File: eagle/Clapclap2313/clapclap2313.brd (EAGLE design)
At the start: 47.9 x 48.2 mm, 20 parts, among them K1 4052, M1 Mic

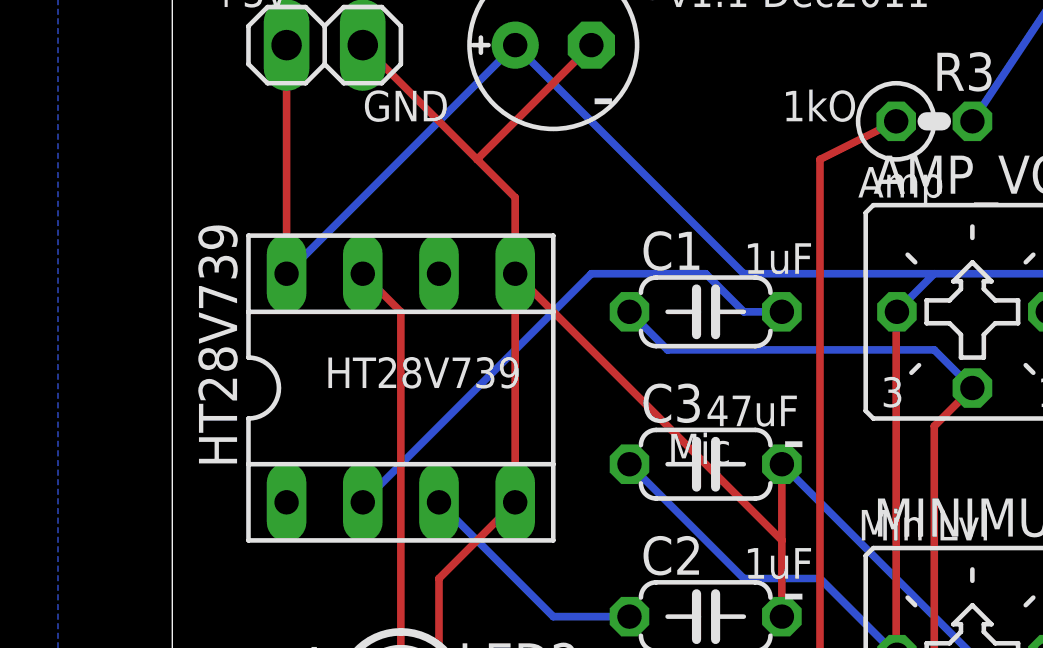
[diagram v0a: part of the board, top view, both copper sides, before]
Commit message: Thanks to Mr. Girts from Riga, the name of the amp is now fixed.
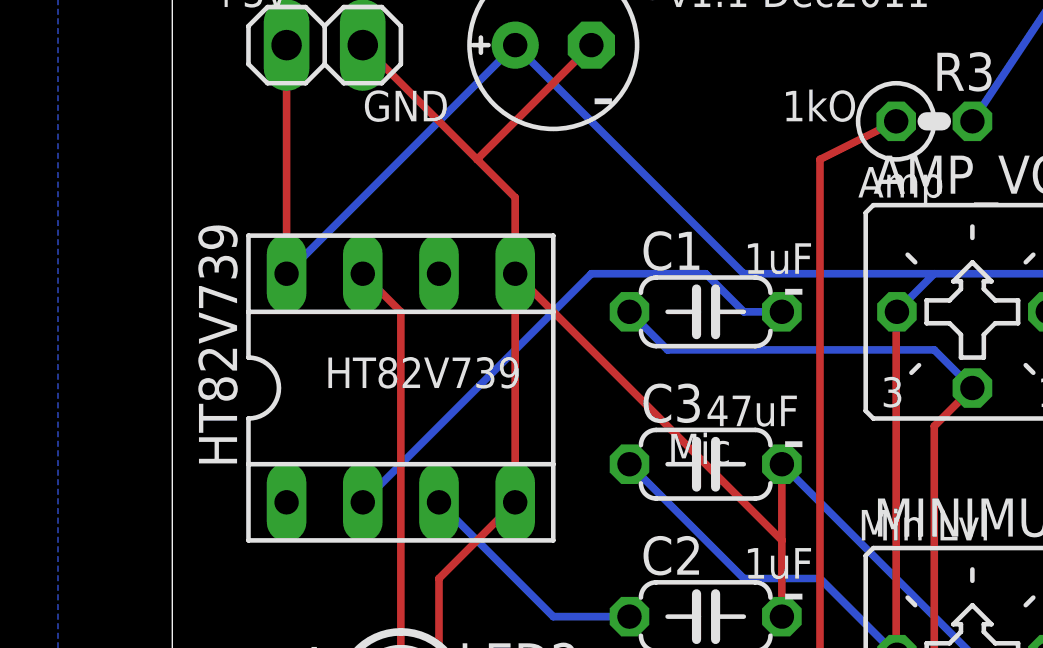
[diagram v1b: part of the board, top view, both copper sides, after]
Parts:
- renumbered HT28V739 to HT82V739
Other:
- board text added: "HT82V739"
- board text removed: "HT28V739"
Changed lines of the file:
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@@
 <text x="6.35" y="41.91" size="1.016" layer="21">GND</text>
 <text x="11.43" y="6.35" size="1.016" layer="21">ATtiny 2313</text>
-<text x="5.08" y="33.02" size="1.016" layer="21">HT28V739</text>
+<text x="5.08" y="33.02" size="1.016" layer="21">HT82V739</text>
 <text x="19.05" y="36.83" size="1.016" layer="21">1uF</text>
 <text x="19.05" y="26.67" size="1.016" layer="21">1uF</text>
@@
 <text x="15.24" y="15.24" size="1.016" layer="21" rot="R90">470o</text>
 <text x="19.05" y="15.24" size="1.016" layer="21" rot="R90">470o</text>
+<text x="20.32" y="35.56" size="1.778" layer="21">-</text>
 </plain>
 <attributes>
@@
 <attribute name="OC_NEWARK" value="unknown" x="16.51" y="6.35" size="1.778" layer="27" display="off"/>
 </element>
-<element name="HT28V739" library="ic-package" package="SOCKET-08" value="" x="7.62" y="33.02"/>
+<element name="HT82V739" library="ic-package" package="SOCKET-08" value="" x="7.62" y="33.02"/>
 <element name="M1" library="pinhead" package="1X02" value="Mic" x="27.94" y="15.24"/>
 <element name="NPN" library="transistor" package="TO92-ECB" value="2SC2120" x="39.37" y="43.18"/>
@@
 <signal name="N$5">
 <contactref element="C1" pad="2"/>
-<contactref element="HT28V739" pad="2"/>
+<contactref element="HT82V739" pad="2"/>
 <wire x1="6.35" y1="29.21" x2="13.97" y2="36.83" width="0.254" layer="16"/>
 <wire x1="13.97" y1="36.83" x2="17.78" y2="36.83" width="0.254" layer="16"/>
@@
 </signal>
 <signal name="N$10">
-<contactref element="HT28V739" pad="7"/>
+<contactref element="HT82V739" pad="7"/>
 <contactref element="ATTINY2313" pad="12"/>
 <wire x1="21.59" y1="6.35" x2="25.4" y2="10.16" width="0.254" layer="1"/>
@@
 <contactref element="AMP_VOL" pad="E"/>
 <contactref element="C3" pad="1"/>
-<contactref element="HT28V739" pad="8"/>
+<contactref element="HT82V739" pad="8"/>
 <contactref element="MINIMUM_LVL" pad="E"/>
 <contactref element="ATTINY2313" pad="20"/>
@@
 <contactref element="AMP_VOL" pad="A"/>
 <contactref element="M1" pad="2"/>
-<contactref element="HT28V739" pad="5"/>
+<contactref element="HT82V739" pad="5"/>
 <contactref element="C2" pad="2"/>
-<contactref element="HT28V739" pad="4"/>
+<contactref element="HT82V739" pad="4"/>
 <contactref element="C3" pad="2"/>
 <contactref element="MINIMUM_LVL" pad="A"/>
@@
 </signal>
 <signal name="N$1">
-<contactref element="HT28V739" pad="3"/>
+<contactref element="HT82V739" pad="3"/>
 <contactref element="C2" pad="1"/>
 <wire x1="8.89" y1="29.21" x2="12.7" y2="25.4" width="0.254" layer="16"/>

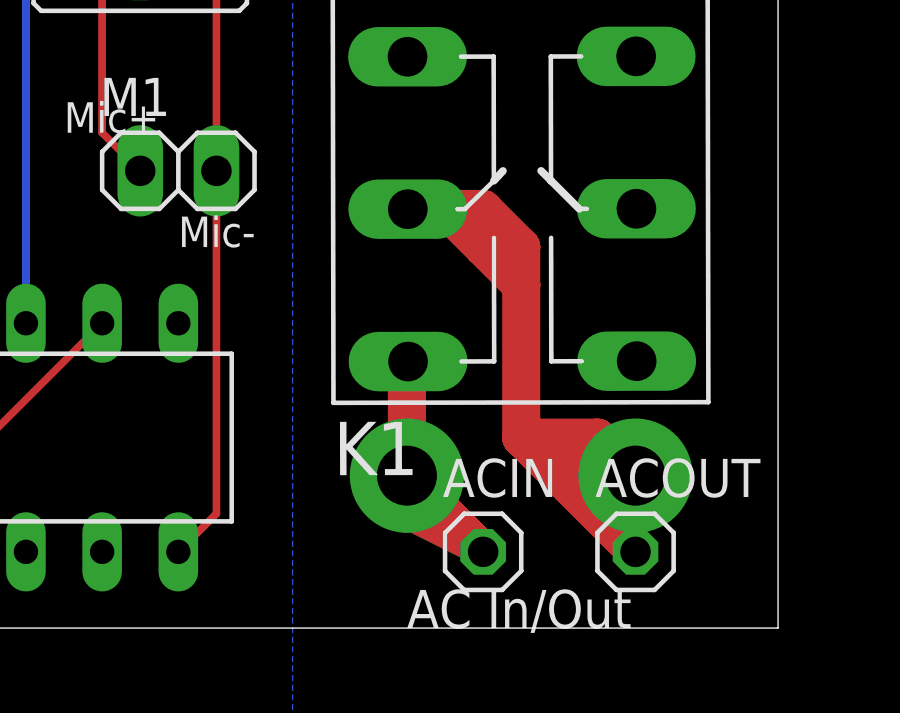
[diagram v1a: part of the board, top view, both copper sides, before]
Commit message: v1.1 final before v1.2. Changed width of some track. Will redo the whole board from scratch to save space in next version.
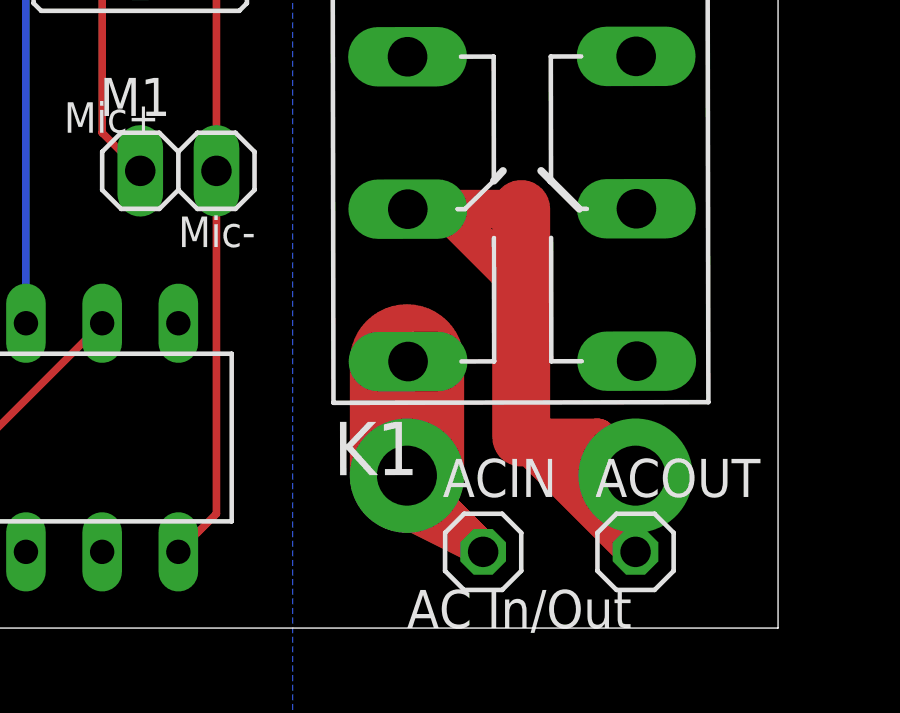
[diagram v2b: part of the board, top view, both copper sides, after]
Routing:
- net ACOUT: track 34.7 -> 31.4 mm
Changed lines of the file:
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@@
 <wire x1="35.56" y1="5.08" x2="35.56" y2="6.35" width="1.016" layer="1"/>
 <wire x1="35.56" y1="6.35" x2="35.597684375" y2="8.88338125" width="1.016" layer="1"/>
-<wire x1="35.56" y1="8.89" x2="35.56" y2="5.08" width="1.27" layer="1"/>
+<wire x1="35.56" y1="8.89" x2="35.56" y2="5.08" width="3.81" layer="1"/>
 <wire x1="35.56" y1="5.08" x2="35.56" y2="3.81" width="1.27" layer="1"/>
 <wire x1="35.56" y1="3.81" x2="36.83" y2="3.81" width="1.27" layer="1"/>
@@
 <wire x1="43.18" y1="2.54" x2="40.64" y2="5.08" width="1.016" layer="1"/>
 <wire x1="40.64" y1="5.08" x2="39.37" y2="6.35" width="1.016" layer="1"/>
-<wire x1="39.37" y1="12.7" x2="36.83" y2="13.97" width="1.016" layer="1"/>
 <wire x1="36.83" y1="13.97" x2="35.58881875" y2="13.963375" width="1.016" layer="1"/>
 <wire x1="39.37" y1="6.35" x2="41.91" y2="6.35" width="1.27" layer="1"/>
 <wire x1="41.91" y1="6.35" x2="40.64" y2="5.08" width="1.27" layer="1"/>
 <wire x1="39.37" y1="6.35" x2="43.18" y2="2.54" width="1.27" layer="1"/>
-<wire x1="39.37" y1="6.35" x2="39.37" y2="11.43" width="1.27" layer="1"/>
-<wire x1="39.37" y1="12.7" x2="38.1" y2="12.7" width="1.27" layer="1"/>
-<wire x1="38.1" y1="12.7" x2="36.83" y2="13.97" width="1.27" layer="1"/>
-<wire x1="38.1" y1="12.7" x2="39.37" y2="11.43" width="1.27" layer="1"/>
-<wire x1="39.37" y1="11.43" x2="39.37" y2="12.7" width="1.27" layer="1"/>
-<wire x1="39.37" y1="12.7" x2="38.1" y2="13.97" width="1.27" layer="1"/>
-<wire x1="38.1" y1="13.97" x2="35.56" y2="13.97" width="1.27" layer="1"/>
+<wire x1="39.37" y1="6.35" x2="39.37" y2="11.43" width="1.9304" layer="1"/>
+<wire x1="39.37" y1="11.43" x2="39.37" y2="13.97" width="1.9304" layer="1"/>
+<wire x1="39.37" y1="11.43" x2="36.83" y2="13.97" width="1.27" layer="1"/>
+<wire x1="39.37" y1="13.97" x2="36.83" y2="13.97" width="1.27" layer="1"/>
+<wire x1="36.83" y1="13.97" x2="35.56" y2="13.97" width="1.27" layer="1"/>
 </signal>
 <signal name="N$13">

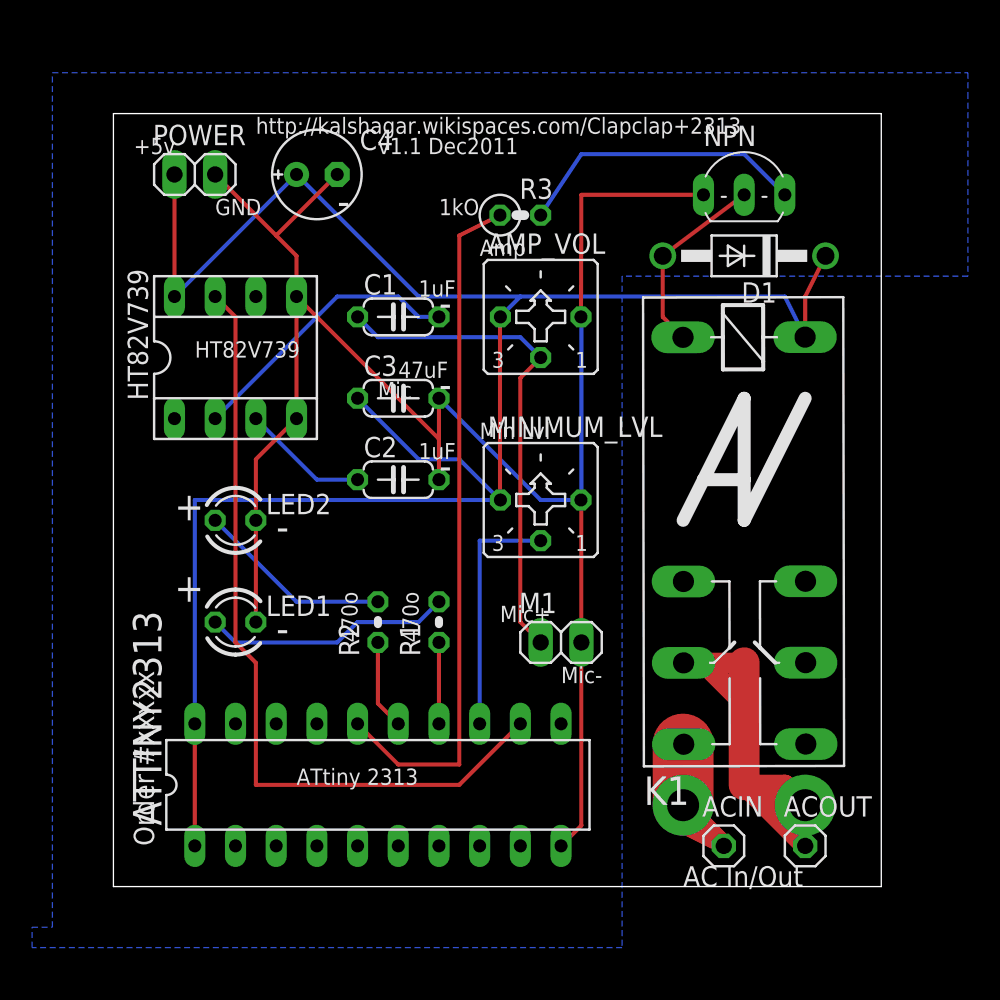
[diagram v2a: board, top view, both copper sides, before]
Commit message: v1.2 : before last labels and check. Made a VCC/AC zone, added pins for AC solder, fat traces to handle amps.
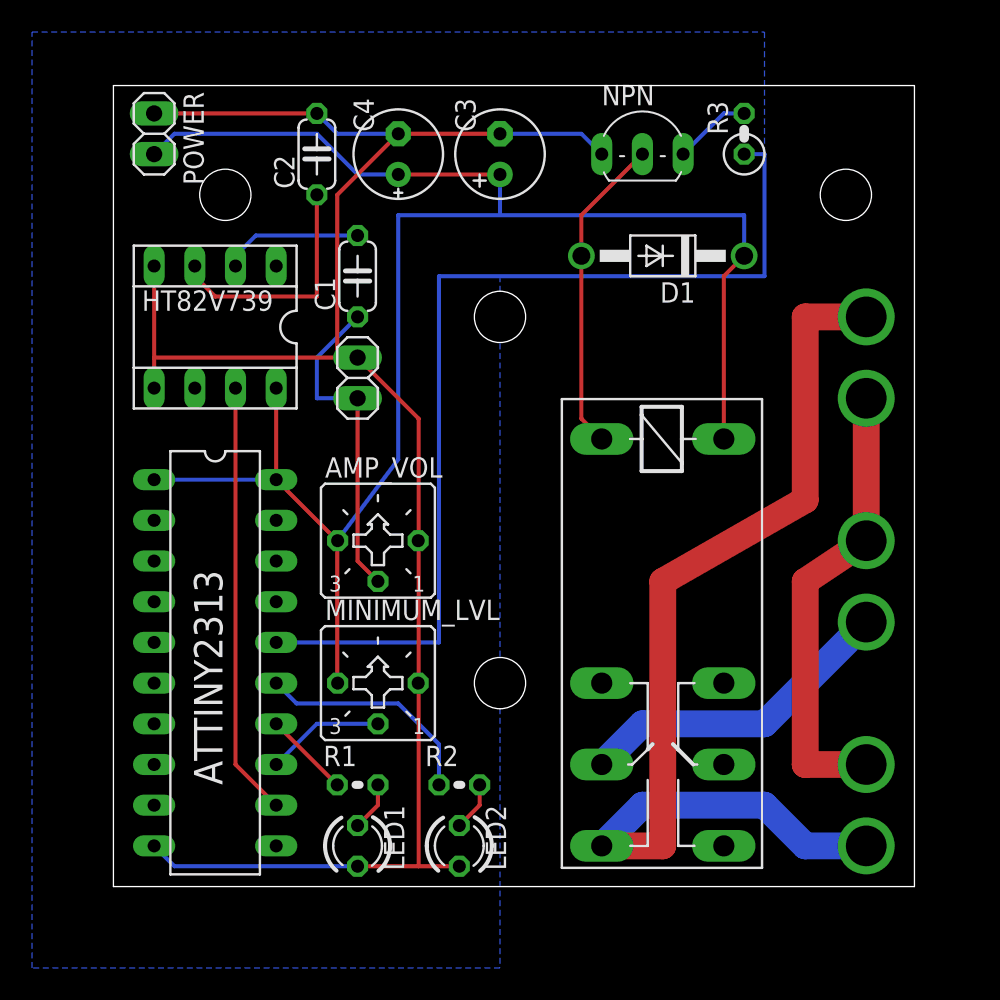
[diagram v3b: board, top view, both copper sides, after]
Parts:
- removed ACIN: (no value), pinhead:1X01
- added LIVE_IN, LIVE_WW, NEUTRAL_IN, NEUTRAL_OUT, NEUTRAL_WW: SPECIAL_DRILL_0.1000, special-drill:PAD_0.1000
- ACOUT: value (none) -> SPECIAL_DRILL_0.1000; device pinhead:1X01 -> special-drill:PAD_0.1000
- C3: device resistor:C050-024X044 -> resistor:E2,5-6
- moved LED2 24.7 mm to (21.6, 2.54), turned to 270 degrees
- moved C2 20.9 mm to (12.7, 45.7), turned to 90 degrees
- moved M1 20.8 mm to (15.2, 31.8), turned to 90 degrees
- moved AMP_VOL 17.3 mm to (16.5, 21.6)
- moved C3 16.5 mm to (24.1, 45.7), turned to 90 degrees
- moved LED1 15.9 mm to (15.2, 2.54), turned to 270 degrees
- moved MINIMUM_LVL 15.3 mm to (16.5, 12.7)
- moved R3 14.9 mm to (39.4, 47.0), turned to 90 degrees
- moved ACOUT 14.5 mm to (47.0, 16.5)
- moved ATTINY2313 12.7 mm to (6.35, 14.0), turned to 270 degrees
- moved R1 11.4 mm to (15.2, 6.35), turned to 0 degrees
- moved R2 11.4 mm to (21.6, 6.35), turned to 0 degrees
- moved K1 8.13 mm to (34.3, 24.1), turned to 270 degrees
- moved NPN 6.84 mm to (33.0, 45.7)
- moved C4 5.24 mm to (17.8, 45.7), turned to 90 degrees
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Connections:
- new net N$13: NEUTRAL_IN.1, NEUTRAL_OUT.1, NEUTRAL_WW.1
- net ACIN: now also LIVE_IN.1, LIVE_WW.1; no longer ACIN.1
- net GND: now also C3.-; no longer C3.2
- net VCC: now also C3.+; no longer C3.1
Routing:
- net ACIN: track 18.4 -> 64.4 mm, vias 1 -> 0
- net N$13: track 0.00 -> 28.7 mm, vias 1 -> 0
- net N$10: track 49.6 -> 27.1 mm
- net N$2: track 43.3 -> 62.2 mm
- net VCC: track 125.7 -> 111.1 mm
- net N$8: track 18.3 -> 4.86 mm
- net N$7: track 15.5 -> 3.07 mm
- net ACOUT: track 31.4 -> 20.2 mm
- net N$3: track 31.3 -> 20.6 mm
- net N$11: track 12.3 -> 3.07 mm
- net N$5: track 17.7 -> 8.78 mm
- net N$6: track 5.61 -> 14.3 mm
- net N$9: track 12.0 -> 19.9 mm
- net N$12: track 15.2 -> 7.40 mm
- net N$1: track 7.93 -> 15.1 mm
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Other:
- board size 47.9 x 48.2 mm -> 50 x 50 mm
- board text added: "Input"
- board text added: "L"
- board text added: "Micro"
- board text added: "N"
- board text added: "Output"
- board text added: "Wallwart"
- board text removed: "+5v"
- board text removed: "1kO"
- board text removed: "1uF"
- board text removed: "470o"
- board text removed: "47uF"
- board text removed: "AC In/Out"
- board text removed: "ATtiny 2313"
- board text removed: "Amp"
- board text removed: "GND"
- board text removed: "HT82V739"
- board text removed: "Mic"
- board text removed: "Mic+"
- board text removed: "Mic-"
- board text removed: "Min Lvl"
- board text removed: "Order #xxxxx"
- board text removed: "http://kalshagar.wikispaces.com/Clapclap+2313"
- board text removed: "v1.1 Dec2011"
